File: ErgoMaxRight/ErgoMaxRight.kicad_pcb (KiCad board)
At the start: 2 copper layers, 182.8 x 169.2 mm, 100 parts, among them J1 PJ-320A, K1 KEYSW, K10 KEYSW, K11 KEYSW, K12 KEYSW, K13 KEYSW, K14 KEYSW, K15 KEYSW, K16 KEYSW, K17 KEYSW, K18 KEYSW, K19 KEYSW, K2 KEYSW, K20 KEYSW, K21 KEYSW, K22 KEYSW, K23 KEYSW, K24 KEYSW, K25 KEYSW, K26 KEYSW, K27 KEYSW, K28 KEYSW, K29 KEYSW, K3 KEYSW, K30 KEYSW, K31 KEYSW, K32 KEYSW, K33 KEYSW, K34 KEYSW, K35 KEYSW, K36 KEYSW, K37 KEYSW, K38 KEYSW, K39 KEYSW, K4 KEYSW, K40 KEYSW, K41 KEYSW, K42 KEYSW, K43 KEYSW, K44 KEYSW, K5 KEYSW, K6 KEYSW, K7 KEYSW, K8 KEYSW, K9 KEYSW, U1 ProMicro

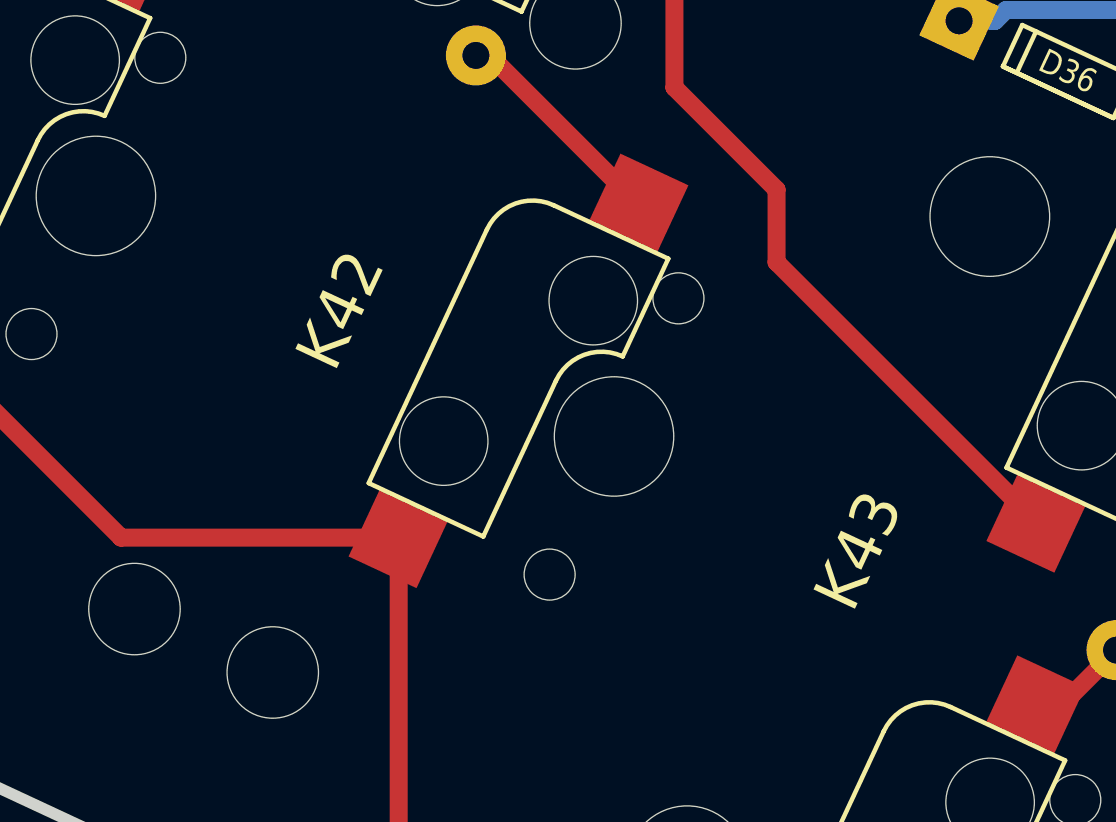
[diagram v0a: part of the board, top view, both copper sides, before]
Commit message: rename footprint library to ErgoMax for clarity
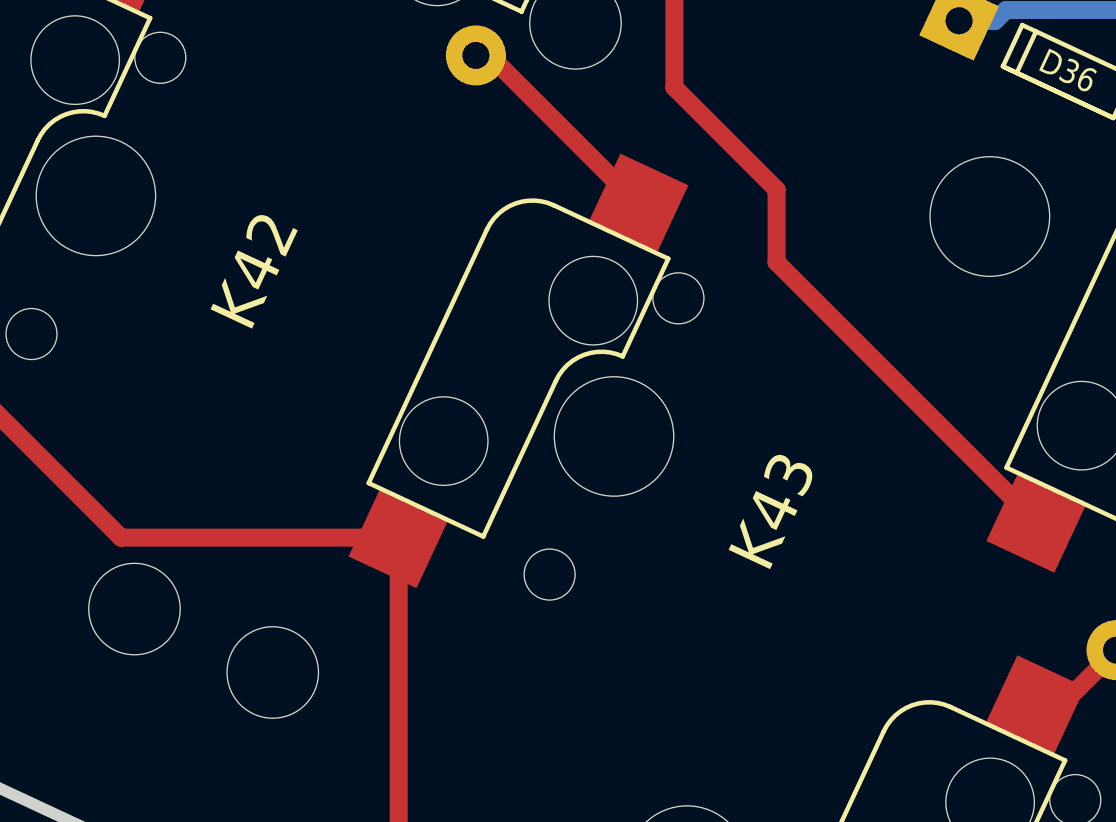
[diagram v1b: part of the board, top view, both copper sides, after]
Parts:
- K1, K10, K11, K12, K13, K14, K15, K16, K17, K18, K19, K2, K20, K21, K22, K23, K24, K25, K26, K27, K28, K29, K3, K30, K31, K32, K33, K34, K35, K36, K37, K38, K39, K4, K40, K41, K42, K43, K44, K5, K6, K7, K8, K9: footprint Kailh_MX_socket:Kailh_MX_Socket -> ErgoMax:Kailh_MX_Socket

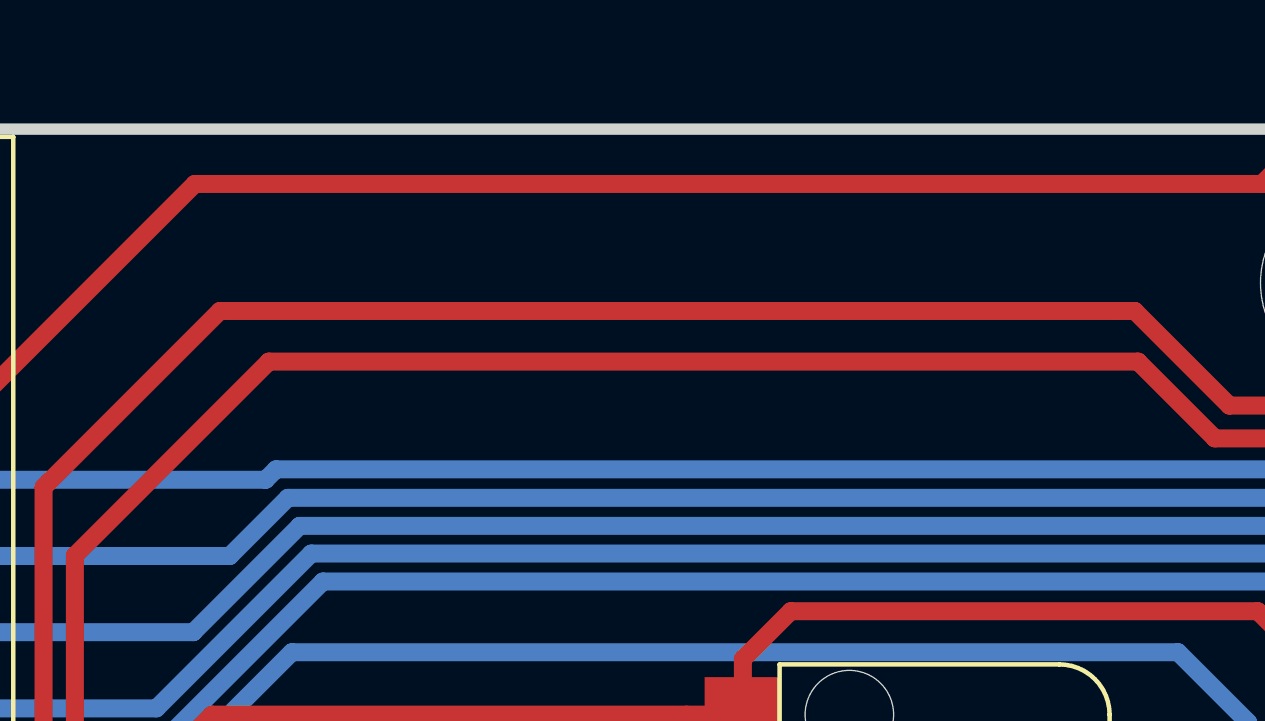
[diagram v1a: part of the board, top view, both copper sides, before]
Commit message: add custom logos in schema and PCB (added them in libs)
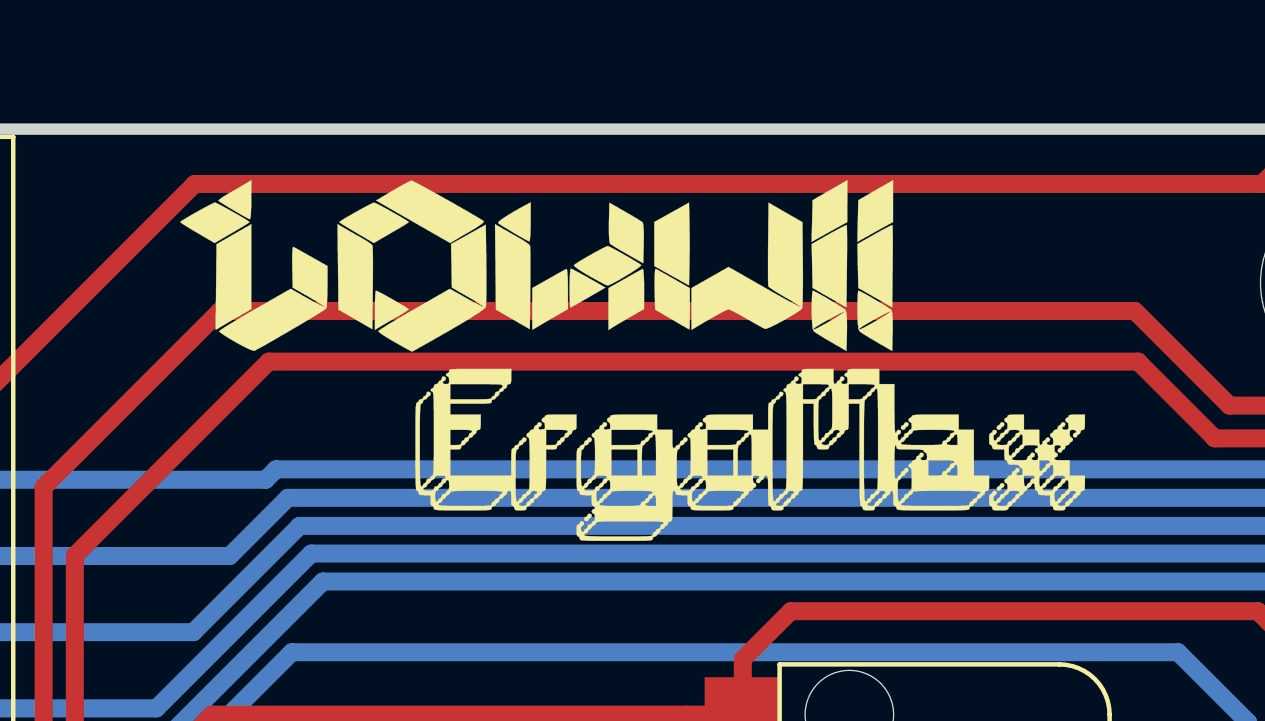
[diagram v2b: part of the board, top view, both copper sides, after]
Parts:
- added Lg1: Logo, ErgoMax:LouWii-logo, F.Cu at (155.1, 40.6)
- added Lg2: Logo, ErgoMax:ErgoMax-logo, F.Cu at (161.8, 46.7)

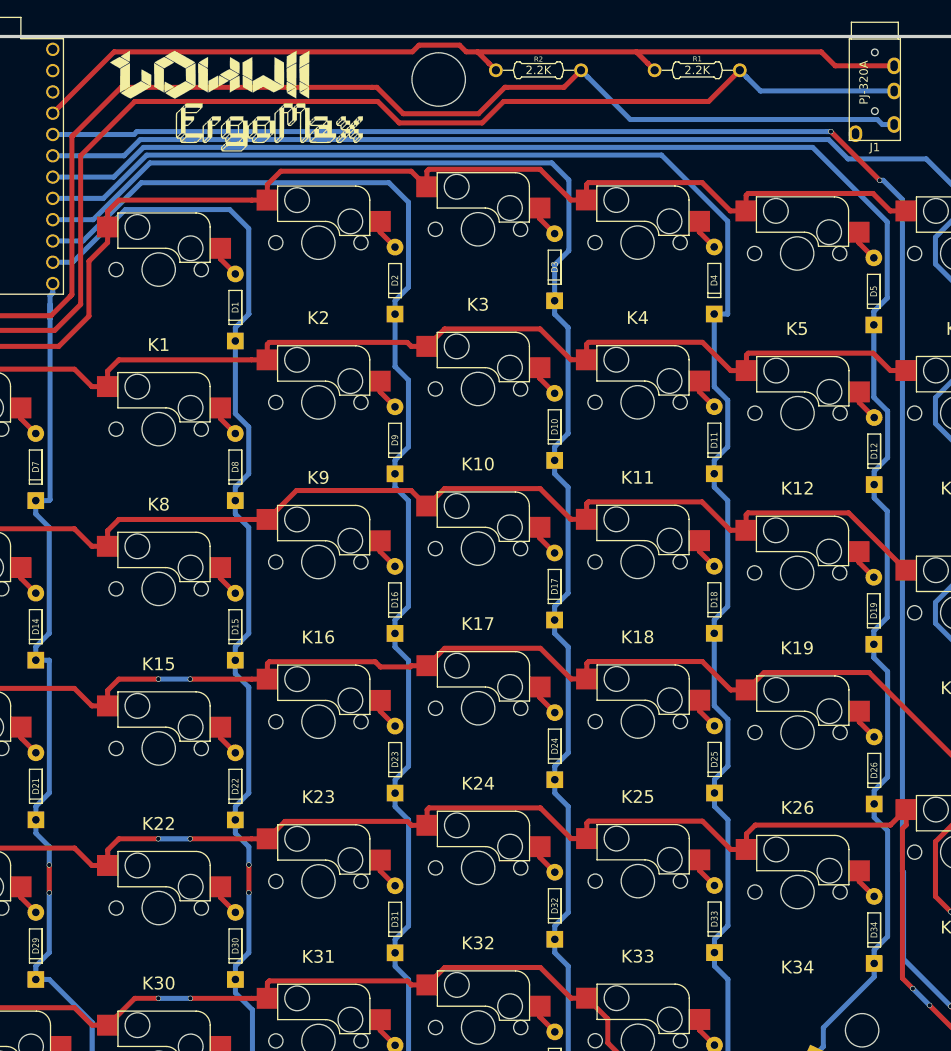
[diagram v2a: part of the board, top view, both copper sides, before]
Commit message: Clean up some wiring and move jack connector to the right side!
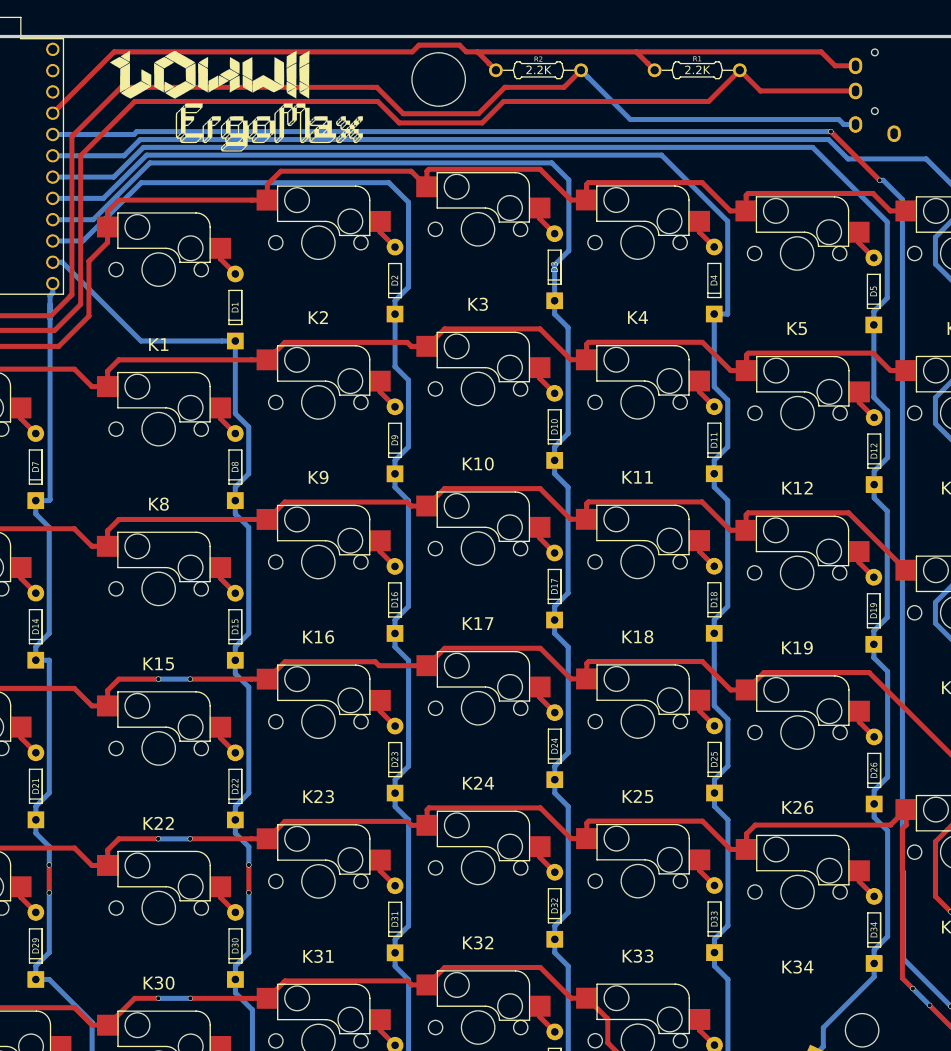
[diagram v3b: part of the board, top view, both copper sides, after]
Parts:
- J1: moved to B.Cu
- turned J1 to 180 degrees
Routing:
- net /Col1: track 143.9 -> 128.5 mm
- net SCL: track 160.7 -> 156.1 mm
- net VCC: track 111.0 -> 106.4 mm
- net SDA: track 163.4 -> 158.8 mm
- net /Row3: track 291.2 -> 289.9 mm
- net /Row2: track 180.2 -> 179.1 mm
- net /Row5: track 283.8 -> 282.7 mm
- net /Row1: track 156.9 -> 155.8 mm
